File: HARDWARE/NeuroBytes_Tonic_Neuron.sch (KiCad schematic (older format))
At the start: 14 parts, among them P1 CONN_01X04, P12 CONN_01X07, U1 STM32L011Gx, U2 LD3985G33R

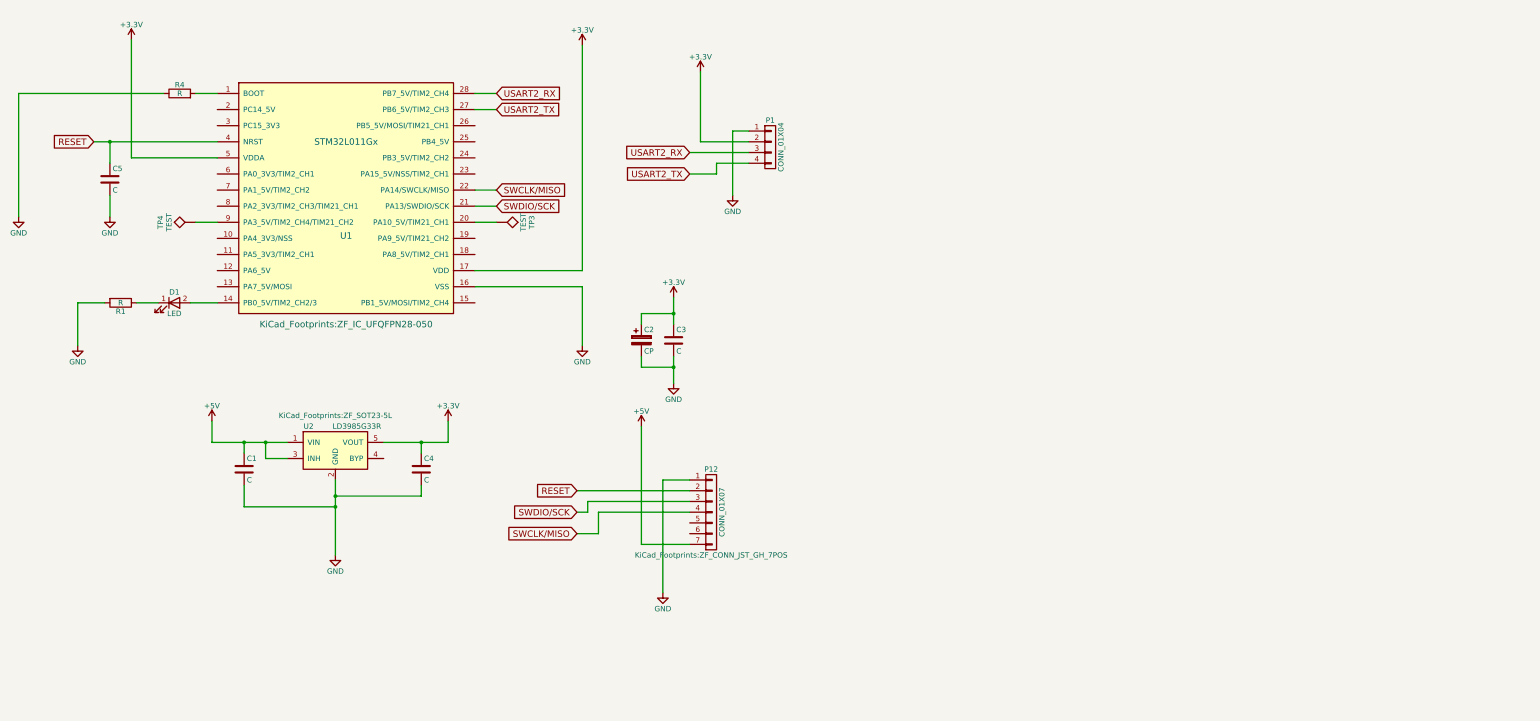
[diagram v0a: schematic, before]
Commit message: fresh clone with current firmware. added new PCB design -- bipolar neuron graphics, etc.
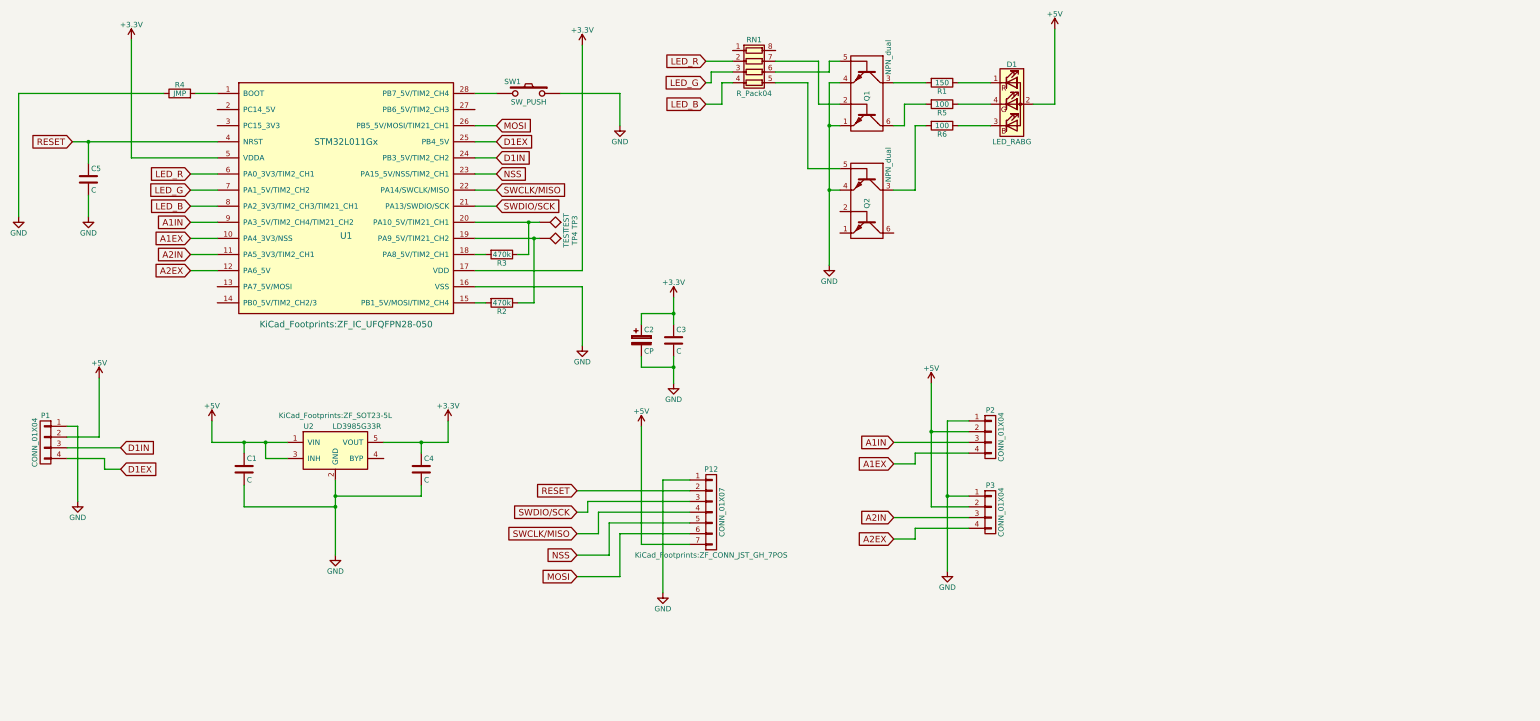
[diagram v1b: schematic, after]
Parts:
- removed D1: LED, KiCad_Footprints:ZF_SMD_pol_0805, symbol LED
- added D1: LED_RABG, KiCad_Footprints:ZF_LED_RGB_SunLED_XZMDKCBDDG45S-9_cast, symbol LED_RABG
- added P2, P3: CONN_01X04, KiCad_Footprints:ZF_CONN_JST_GH, symbol CONN_01X04
- added Q1, Q2: NPN_dual, KiCad_Footprints:ZF_SMD_SOT-363, symbol NPN_dual
- added R2, R3: 470k, KiCad_Footprints:ZF_SMD_NonPol_0402, symbol R
- added R5, R6: 100, KiCad_Footprints:ZF_SMD_NonPol_0402, symbol R
- added RN1: R_Pack04, KiCad_Footprints:ZF_RN_4iso_CTS-0804, symbol R_Pack04
- added SW1: SW_PUSH, KiCad_Footprints:ZF_SW_Momentary_SideMtg, symbol SW_PUSH
- P1: footprint KiCad_Footprints:ZF_CONN_1x4-hdr -> KiCad_Footprints:ZF_CONN_JST_GH
- R1: value R -> 150
- R4: value R -> JMP
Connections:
- net +3V3: no longer P1.2 (P2)
- net +5V: now also P1.2 (P2), D1.2 (A), P2.2 (P2), P3.2 (P2)
- net GND: now also P2.1 (P1), P3.1 (P1), Q1.1, Q1.4, Q2.4, SW1.1; no longer R1.2
- net A1EX: now reaches U1.10 (PA4_3V3/NSS)
- net A1EX: now also P2.4 (P4)
- net A2IN: now reaches U1.11 (PA5_3V3/TIM2_CH1)
- net A2IN: now also P3.3 (P3)
- net A2EX: now reaches U1.12 (PA6_5V)
- net A2EX: now also P3.4 (P4)
- net at U1.15 (PB1_5V/MOSI/TIM2_CH4): now also R2.2
- net at U1.18 (PA8_5V/TIM2_CH1): now also R3.2
- net at U1.19 (PA9_5V/TIM21_CH2): now also TP4.1, R2.1
- net at TP3.1, U1.20 (PA10_5V/TIM21_CH1): now also R3.1
- net NSS: now reaches U1.23 (PA15_5V/NSS/TIM2_CH1)
- net NSS: now also P12.5 (P5)
- net D1IN: now reaches U1.24 (PB3_5V/TIM2_CH2)
- net D1IN: now also P1.3 (P3)
- net D1EX: now reaches U1.25 (PB4_5V)
- net D1EX: now also P1.4 (P4)
- net MOSI: now reaches U1.26 (PB5_5V/MOSI/TIM21_CH1)
- net MOSI: now also P12.6 (P6)
- net LED_R: now reaches U1.6 (PA0_3V3/TIM2_CH1)
- net LED_R: now also RN1.2 (R2.1)
- net LED_G: now reaches U1.7 (PA1_5V/TIM2_CH2)
- net LED_G: now also RN1.3 (R3.1)
- net LED_B: now reaches U1.8 (PA2_3V3/TIM2_CH3/TIM21_CH1)
- net LED_B: now also RN1.4 (R4.1)
- net A1IN: now reaches U1.9 (PA3_5V/TIM2_CH4/TIM21_CH2)
- net A1IN: now also P2.3 (P3); no longer TP4.1
- net at R1.1: now also D1.1 (RK)
- net USART2_RX: no longer names the net of U1.28 (PB7_5V/TIM2_CH4)
- net USART2_RX: now also SW1.2; no longer P1.3 (P3)
- net USART2_TX: no longer names the net of U1.27 (PB6_5V/TIM2_CH3)
- net USART2_TX: no longer P1.4 (P4)
- new net: Q2.5 (BASE1), RN1.5 (R4.2)
- new net: Q1.5 (BASE1), RN1.6 (R3.2)
- new net: Q1.2 (BASE2), RN1.7 (R2.2)
- new net: Q1.3, R1.2
- new net: Q1.6, R5.2
- new net: Q2.3, R6.2
- new net: D1.3 (BK), R6.1
- new net: D1.4 (GK), R5.1
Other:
- moved on the sheet: C5, TP3, TP4

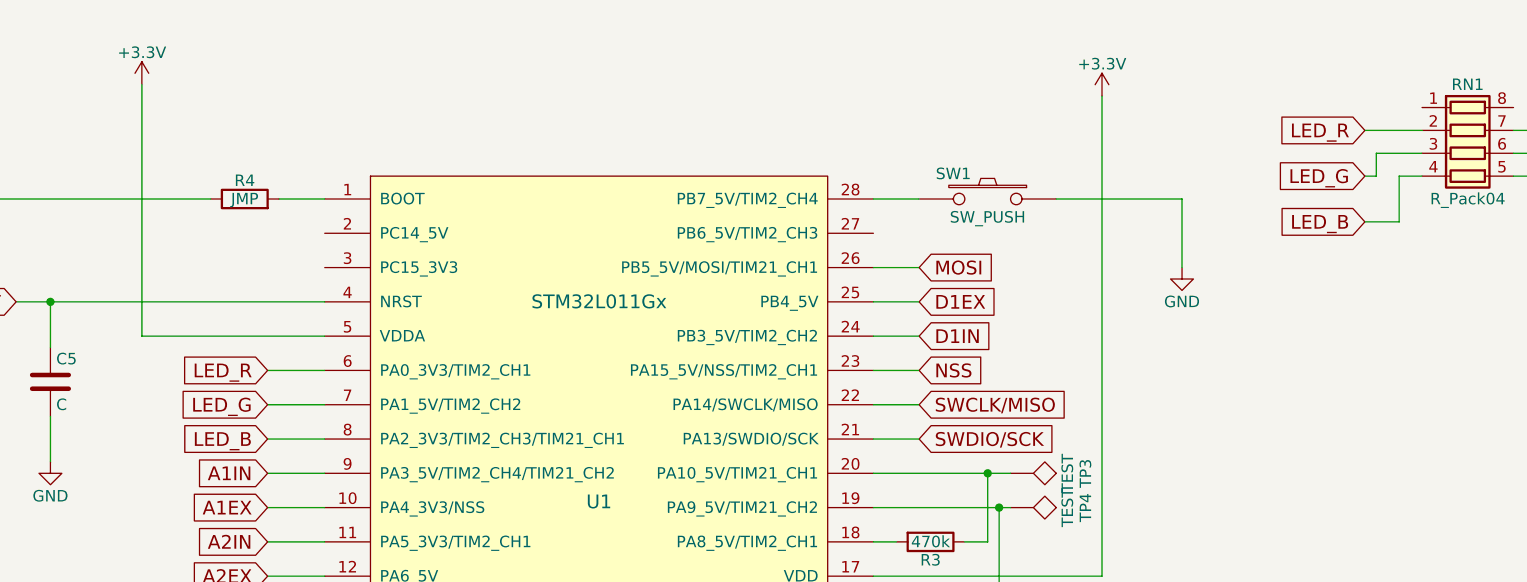
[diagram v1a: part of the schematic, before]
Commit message: removed miniprintf stuff. updated firmware for new board with external resistors for touch slider. currently runs test program that maps finger position to blue LED color.
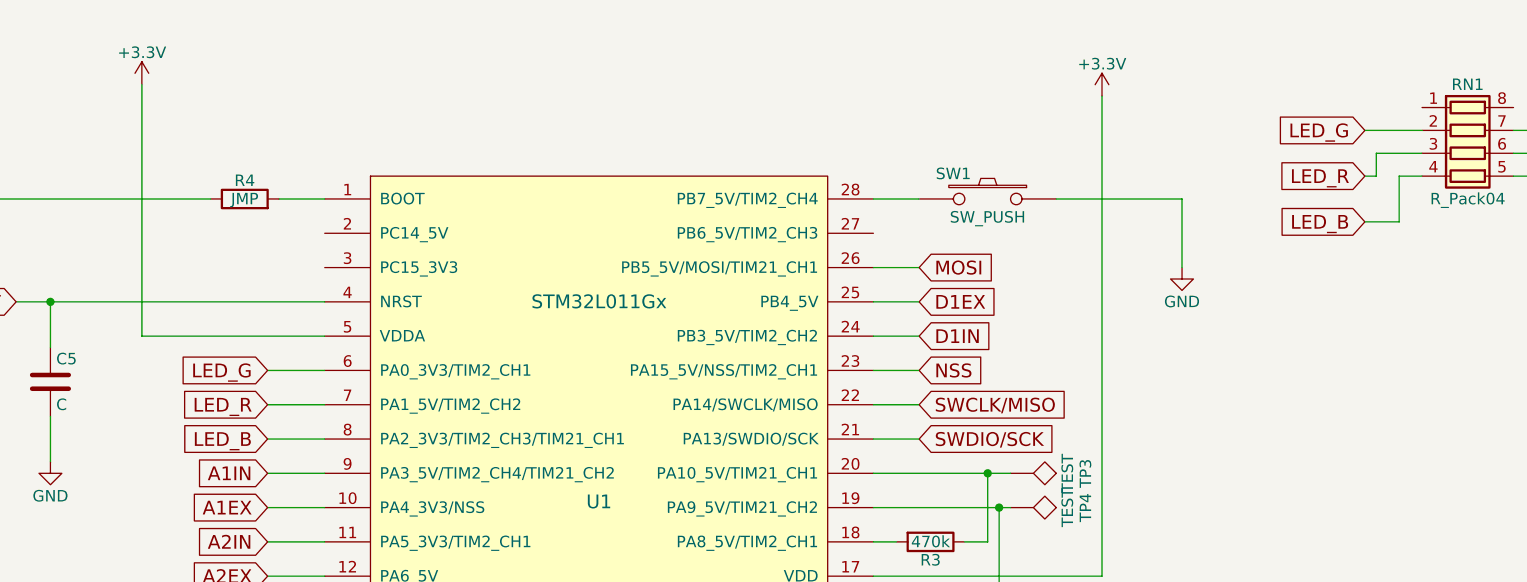
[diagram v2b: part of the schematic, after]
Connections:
- net LED_G: now also RN1.2 (R2.1), U1.6 (PA0_3V3/TIM2_CH1); no longer RN1.3 (R3.1), U1.7 (PA1_5V/TIM2_CH2)
- net LED_R: now also RN1.3 (R3.1), U1.7 (PA1_5V/TIM2_CH2); no longer RN1.2 (R2.1), U1.6 (PA0_3V3/TIM2_CH1)
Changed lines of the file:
@@
 Wire Wire Line
 	6550 6000 6150 6000
+Text GLabel 2550 2400 0    60   Input ~ 0
+LED_R
 Text GLabel 2550 2250 0    60   Input ~ 0
-LED_R
-Text GLabel 2550 2400 0    60   Input ~ 0
 LED_G
 Text GLabel 2550 2550 0    60   Input ~ 0
@@
 Wire Wire Line
 	2550 2550 2800 2550
+Text GLabel 7350 1400 0    60   Input ~ 0
+LED_R
 Text GLabel 7350 1200 0    60   Input ~ 0
-LED_R
-Text GLabel 7350 1400 0    60   Input ~ 0
 LED_G
 Text GLabel 7350 1600 0    60   Input ~ 0

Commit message: changed to 5-pin JST GH connector for power / prog
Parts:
- removed P12: CONN_01X07, KiCad_Footprints:ZF_CONN_JST_GH_7POS, symbol CONN_01X07
- added P4: JST_GH_5-pos, KiCad_Footprints:ZF_CONN_JST_GH_5POS, symbol CONN_01X05
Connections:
- net +5V: now also P4.5 (P5)
- net A1EX: now also U1.12 (PA6_5V); no longer U1.10 (PA4_3V3/NSS)
- net A1IN: now also U1.11 (PA5_3V3/TIM2_CH1); no longer U1.9 (PA3_5V/TIM2_CH4/TIM21_CH2)
- net A2EX: now also U1.14 (PB0_5V/TIM2_CH2/3); no longer U1.12 (PA6_5V)
- net A2IN: now also U1.13 (PA7_5V/MOSI); no longer U1.11 (PA5_3V3/TIM2_CH1)
- net GND: now also P4.1 (P1)
- net RESET: now also P4.2 (P2)
- net MOSI: no longer names the net of U1.26 (PB5_5V/MOSI/TIM21_CH1)
- net NSS: no longer names the net of U1.23 (PA15_5V/NSS/TIM2_CH1)
- net SWCLK/MISO renamed SWCLK
- net SWCLK: now also P4.4 (P4)
- net SWDIO/SCK renamed SWDIO
- net SWDIO: now also P4.3 (P3)
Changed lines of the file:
@@
 	1450 1950 2800 1950
 Text GLabel 5400 2400 2    60   Input ~ 0
-SWCLK/MISO
+SWCLK
 Wire Wire Line
 	6200 3150 6200 1050
@@
 	5400 2400 5200 2400
 Text GLabel 5400 2550 2    60   Input ~ 0
-SWDIO/SCK
+SWDIO
 Wire Wire Line
 	5400 2550 5200 2550
@@
 Connection ~ 7050 3550
 $Comp
-L CONN_01X07 P12
-U 1 1 58B5DF5E
-P 7400 5400
-F 0 "P12" H 7400 5800 50  0000 C CNN
-F 1 "CONN_01X07" V 7500 5400 50  0000 C CNN
-F 2 "KiCad_Footprints:ZF_CONN_JST_GH_7POS" H 7400 5000 50  0000 C CNN
-F 3 "" H 7400 5400 50  0000 C CNN
-F 4 "No" H 7400 5400 60  0001 C CNN "Subs Allowed"
-F 5 "Yes" H 7400 5400 60  0001 C CNN "RoHS"
-	1    7400 5400
-	1    0    0    -1
-$EndComp
-$Comp
 L GND #PWR09
 U 1 1 58B5E0E3
@@
 	1    0    0    -1
 $EndComp
-Wire Wire Line
-	6750 4600 6750 5700
-Wire Wire Line
-	6750 5700 7200 5700
 Text GLabel 6150 5200 0    60   Input ~ 0
 RESET
@@
 	6150 5200 7200 5200
 Text GLabel 6150 5600 0    60   Input ~ 0
-SWCLK/MISO
+SWCLK
 Text GLabel 6150 5400 0    60   Input ~ 0
-SWDIO/SCK
+SWDIO
 Wire Wire Line
 	6150 5600 6350 5600
@@
 Wire Wire Line
 	9300 5550 9800 5550
-Text GLabel 5400 2250 2    60   Input ~ 0
-NSS
-Wire Wire Line
-	5400 2250 5200 2250
-Text GLabel 5400 1800 2    60   Input ~ 0
-MOSI
-Wire Wire Line
-	5400 1800 5200 1800
 Wire Wire Line
 	5400 2100 5200 2100
-Text GLabel 2550 2700 0    60   Input ~ 0
+Text GLabel 2550 3000 0    60   Input ~ 0
 A1IN
-Text GLabel 2550 2850 0    60   Input ~ 0
+Text GLabel 2550 3150 0    60   Input ~ 0
 A1EX
 Wire Wire Line
 	5400 1950 5200 1950
-Text GLabel 2550 3000 0    60   Input ~ 0
+Text GLabel 2550 3300 0    60   Input ~ 0
 A2IN
-Text GLabel 2550 3150 0    60   Input ~ 0
+Text GLabel 2550 3450 0    60   Input ~ 0
 A2EX
-Text GLabel 6150 5800 0    60   Input ~ 0
-NSS
-Text GLabel 6150 6000 0    60   Input ~ 0
-MOSI
-Wire Wire Line
-	6150 5800 6450 5800
-Wire Wire Line
-	6450 5800 6450 5500
-Wire Wire Line
-	6450 5500 7200 5500
-Wire Wire Line
-	7200 5600 6550 5600
-Wire Wire Line
-	6550 5600 6550 6000
-Wire Wire Line
-	6550 6000 6150 6000
 Text GLabel 2550 2400 0    60   Input ~ 0
 LED_R
@@
 Connection ~ 5750 2850
 Wire Wire Line
-	2550 3150 2800 3150
-Wire Wire Line
-	2550 3000 2800 3000
-Wire Wire Line
-	2550 2850 2800 2850
-Wire Wire Line
-	2550 2700 2800 2700
-Wire Wire Line
 	8300 2200 8300 1400
 Connection ~ 8500 2400
@@
 	5400 1500 5200 1500
 $Comp
-L GND #PWR?
+L GND #PWR019
 U 1 1 5955279D
 P 6550 1800
-F 0 "#PWR?" H 6550 1550 50  0001 C CNN
+F 0 "#PWR019" H 6550 1550 50  0001 C CNN
 F 1 "GND" H 6550 1650 50  0000 C CNN
 F 2 "" H 6550 1800 50  0000 C CNN
@@
 Wire Wire Line
 	6550 1500 6000 1500
+Wire Wire Line
+	6750 4600 6750 5500
+Wire Wire Line
+	6750 5500 7200 5500
+$Comp
+L CONN_01X05 P4
+U 1 1 598E1AC8
+P 7400 5300
+F 0 "P4" H 7400 5600 50  0000 C CNN
+F 1 "JST_GH_5-pos" V 7500 5300 50  0000 C CNN
+F 2 "KiCad_Footprints:ZF_CONN_JST_GH_5POS" H 7750 4950 50  0000 C CNN
+F 3 "" H 7400 5300 50  0000 C CNN
+F 4 "No" H 7400 5300 60  0001 C CNN "Subs Allowed"
+F 5 "Yes" H 7400 5300 60  0001 C CNN "RoHS"
+	1    7400 5300
+	1    0    0    -1
+$EndComp
+Wire Wire Line
+	2550 3000 2800 3000
+Wire Wire Line
+	2550 3150 2800 3150
+Wire Wire Line
+	2550 3300 2800 3300
+Wire Wire Line
+	2550 3450 2800 3450
 $EndSCHEMATC

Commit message: changed to single NPN transitors and non-networked resistors. still need to finish routing.
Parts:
- removed C2: CP, KiCad_Footprints:ZF_SMD_pol_1206, symbol CP
- removed Q1, Q2: NPN_dual, KiCad_Footprints:ZF_SMD_SOT-363, symbol NPN_dual
- removed RN1: R_Pack04, KiCad_Footprints:ZF_RN_4iso_CTS-0804, symbol R_Pack04
- added C2: 10u, KiCad_Footprints:ZF_SMD_nonpol_1206, symbol C
- added Q1, Q2, Q3: Q_NPN_BEC, KiCad_Footprints:ZF_SOT23-3L, symbol Q_NPN_BEC
- added R7, R8, R9: 1k, KiCad_Footprints:ZF_SMD_NonPol_0402, symbol R
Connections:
- wire segments 118 -> 111
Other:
- moved on the sheet: D1, R1, R5, R6

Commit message: updated BOM labels. missing link and part number for R2 and R3.
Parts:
- C1, C4: value C -> 1u; Link (none) -> https://www.digikey.com/product-detail/en/taiyo-yuden/LMK10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; Mfr (none) -> Taiyo Yuden; Mfr Part # (none) -> LMK107B7105KA-T; Package (none) -> C0603; Subs Allowed No -> Yes
- C2: Link (none) -> https://www.digikey.com/product-detail/en/taiyo-yuden/EMK31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; Mfr (none) -> Taiyo Yuden; Mfr Part # (none) -> EMK316B7106KL-TD; Package (none) -> C1206; Subs Allowed No -> Yes
- C3, C5: value C -> 0u1; Link (none) -> https://www.digikey.com/product-detail/en/taiyo-yuden/LMK10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; Mfr (none) -> Taiyo Yuden; Mfr Part # (none) -> LMK105BJ104KV-F; Package (none) -> C0402; Subs Allowed No -> Yes
- D1: Link (none) -> https://www.digikey.com/product-detail/en/sunled/XZMDKCBDDG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; Mfr (none) -> SunLED; Mfr Part # (none) -> XZMDKCBDDG45S-9; Package (none) -> SMT
- P1, P2, P3: Link (none) -> https://www.digikey.com/product-detail/en/jst-sales-america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; Mfr (none) -> JST; Mfr Part # (none) -> SM04B-GHS-TB(LF)(SN); Package (none) -> SMT
- P4: Link (none) -> https://www.digikey.com/product-detail/en/jst-sales-america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; Mfr (none) -> JST; Mfr Part # (none) -> SM05B-GHS-TB(LF)(SN); Package (none) -> SMT
- Q1, Q2, Q3: Link (none) -> https://www.digikey.com/product-detail/en/micro-commercial-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; Mfr (none) -> Micro Commercial Co; Mfr Part # (none) -> MMBT3904-TP; Package (none) -> SOT23-3; Subs Allowed No -> Yes
- R1: Link (none) -> https://www.digikey.com/product-detail/en/yageo/RC0402FR-07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; Mfr (none) -> Yageo; Mfr Part # (none) -> RC0402FR-07150RL; Package (none) -> R0402; Subs Allowed No -> Yes
- R2, R3: Link (none) -> TBD; Mfr (none) -> Yageo; Mfr Part # (none) -> TBD; Package (none) -> R0402; Subs Allowed No -> Yes
- R4: Link (none) -> https://www.digikey.com/product-detail/en/yageo/RC0402JR-07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; Mfr (none) -> Yageo; Mfr Part # (none) -> RC0402JR-070RL; Package (none) -> R0402; Subs Allowed No -> Yes
- R5, R6: Link (none) -> https://www.digikey.com/product-detail/en/yageo/RC0402FR-07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; Mfr (none) -> Yageo; Mfr Part # (none) -> RC0402FR-07100RL; Package (none) -> R0402; Subs Allowed No -> Yes
- R7, R8, R9: Link (none) -> https://www.digikey.com/product-detail/en/yageo/RC0402FR-07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; Mfr (none) -> Yageo; Mfr Part # (none) -> RC0402FR-071KL; Package (none) -> R0402; Subs Allowed No -> Yes
- SW1: Link (none) -> https://www.digikey.com/product-detail/en/e-switch/TL3330AF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; Mfr (none) -> E-Switch; Mfr Part # (none) -> TL3330AF130QG; Package (none) -> SMT
- U1: Link (none) -> http://www.mouser.com/ProductDetail/STMicroelectronics/STM3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; Mfr (none) -> ST Microelectronics; Mfr Part # (none) -> STM32L011G4U6; Package (none) -> 28-UFQFN
- U2: Link (none) -> https://www.digikey.com/product-detail/en/on-semiconductor/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; Mfr (none) -> ON Semiconductor; Mfr Part # (none) -> NCP114BSN330T1G; Package (none) -> SOT-23-5; Subs Allowed No -> Yes

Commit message: minor page layout updates
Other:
- note added: "AXON TERMINAL"
- note added: "BYPASS CAPS"
- note added: "DENDRITE"
- note added: "LED"
- note added: "MICROCONTROLLER"
- note added: "POWER SUPPLY"
- note added: "POWER/PROGRAMMING CONNECTOR"
- moved on the sheet: C1, C2, C3, C4, D1, P1, P2, P3, P4, R1, R5, R6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

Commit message: BOM updates. Regenerated netlist.
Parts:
- R2, R3: Link TBD -> https://www.digikey.com/product-detail/en/yageo/RC0402FR-07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; Mfr Part # TBD -> RC0402FR-07470KL
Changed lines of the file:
@@
 F 3 "" H 5450 3000 50  0000 C CNN
 F 4 "Yageo" H 5450 3000 60  0001 C CNN "Mfr"
-F 5 "TBD" H 5450 3000 60  0001 C CNN "Mfr Part #"
+F 5 "RC0402FR-07470KL " H 5450 3000 60  0001 C CNN "Mfr Part #"
 F 6 "R0402" H 5450 3000 60  0001 C CNN "Package"
-F 7 "TBD" H 5450 3000 60  0001 C CNN "Link"
+F 7 "https://www.digikey.com/product-detail/en/yageo/RC0402FR-07470KL/311-470KLRTR-ND/726618" H 5450 3000 60  0001 C CNN "Link"
 F 8 "Yes" H 5450 3000 60  0001 C CNN "Subs Allowed"
 F 9 "Yes" H 5450 3000 60  0001 C CNN "RoHS"
@@
 	1    0    0    -1
 $EndComp
-$Comp
-L R R2
-U 1 1 59D15AB0
-P 5450 3450
-F 0 "R2" V 5530 3450 50  0000 C CNN
-F 1 "470k" V 5450 3450 50  0000 C CNN
-F 2 "KiCad_Footprints:ZF_SMD_NonPol_0402" V 5380 3450 50  0001 C CNN
-F 3 "" H 5450 3450 50  0000 C CNN
-F 4 "Yageo" H 5450 3450 60  0001 C CNN "Mfr"
-F 5 "TBD" H 5450 3450 60  0001 C CNN "Mfr Part #"
-F 6 "R0402" H 5450 3450 60  0001 C CNN "Package"
-F 7 "TBD" H 5450 3450 60  0001 C CNN "Link"
-F 8 "Yes" H 5450 3450 60  0001 C CNN "Subs Allowed"
-F 9 "Yes" H 5450 3450 60  0001 C CNN "RoHS"
-	1    5450 3450
-	0    1    1    0
-$EndComp
 Text Notes 3450 1200 0    60   ~ 0
 MICROCONTROLLER
@@
 Text Notes 13750 3700 0    60   ~ 0
 AXON TERMINAL
+$Comp
+L R R2
+U 1 1 59D51BA8
+P 5450 3450
+F 0 "R2" V 5530 3450 50  0000 C CNN
+F 1 "470k" V 5450 3450 50  0000 C CNN
+F 2 "KiCad_Footprints:ZF_SMD_NonPol_0402" V 5380 3450 50  0001 C CNN
+F 3 "" H 5450 3450 50  0000 C CNN
+F 4 "Yageo" H 5450 3450 60  0001 C CNN "Mfr"
+F 5 "RC0402FR-07470KL " H 5450 3450 60  0001 C CNN "Mfr Part #"
+F 6 "R0402" H 5450 3450 60  0001 C CNN "Package"
+F 7 "https://www.digikey.com/product-detail/en/yageo/RC0402FR-07470KL/311-470KLRTR-ND/726618" H 5450 3450 60  0001 C CNN "Link"
+F 8 "Yes" H 5450 3450 60  0001 C CNN "Subs Allowed"
+F 9 "Yes" H 5450 3450 60  0001 C CNN "RoHS"
+	1    5450 3450
+	0    1    1    0
+$EndComp
 $EndSCHEMATC

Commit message: changed to RClamp0503F for ESD protection (touch slider, switch, 3v3). ordered 30 PCBs.
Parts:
- removed U2: LD3985G33R, KiCad_Footprints:ZF_SOT23-5L, symbol LD3985G33R
- added U2: TLV70033_SOT23-5, KiCad_Footprints:ZF_SOT23-5L, symbol TLV70033_SOT23-5
- added U3: RClamp0503F, KiCad_Footprints:ZF_SMD_SOT-353, symbol RClamp0503F
- P1, P2, P3: symbol CONN_01X04 -> Conn_01x04
- P4: symbol CONN_01X05 -> Conn_01x05
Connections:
- wire segments 111 -> 120
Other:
- moved on the sheet: D1, R1, R5, R6, R7, R8, R9, SW1, TP3, TP4
